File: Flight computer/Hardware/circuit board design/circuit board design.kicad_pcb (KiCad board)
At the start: 4 copper layers, 82.5 x 31.8 mm, 106 parts, among them J1 Conn_01x04, J2 USB_B_Micro, J3 Conn_01x02, Q1 Q_PMOS_DGS, U1 IIS2MDC, U10 BMI088, U11 ATSAML21J18B-AUT, U12 MAX2659ELT+, U13 SAFEB1G57KE0F00, U2 AS179-92LF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

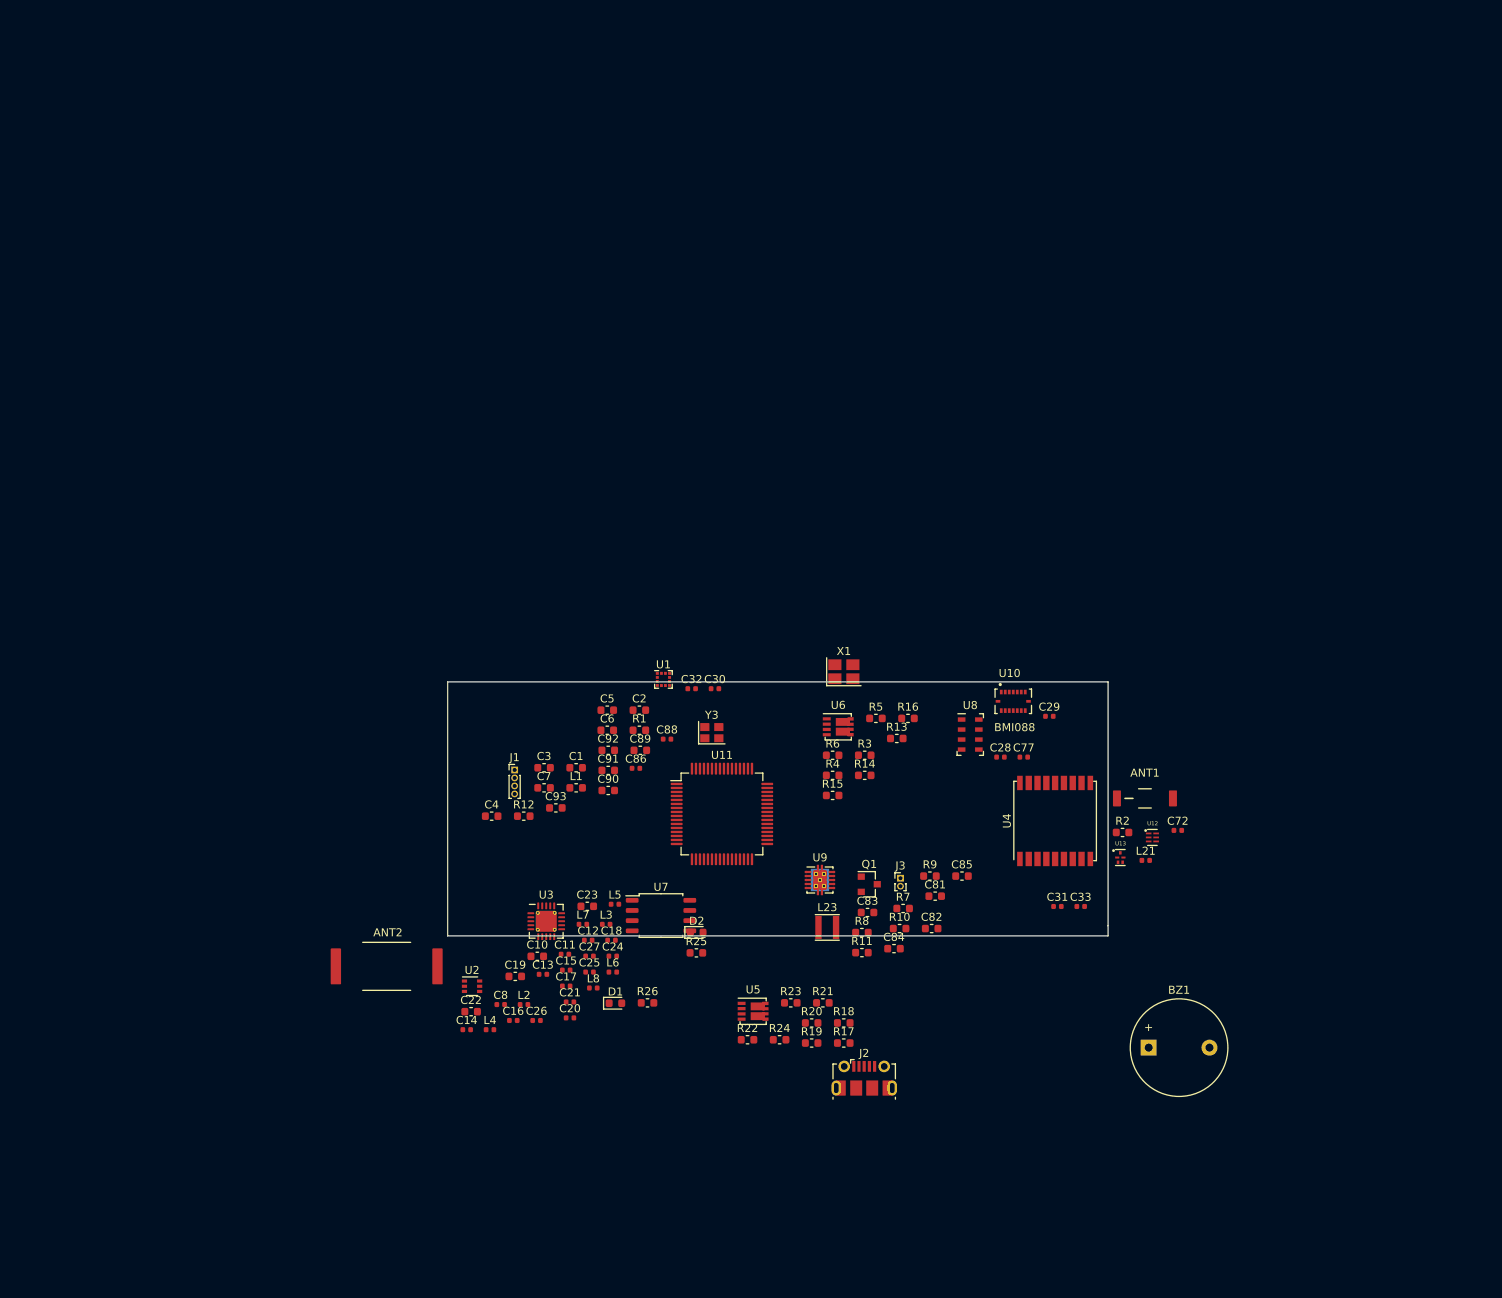
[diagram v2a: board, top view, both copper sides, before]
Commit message: set up the PCB to fit formfactor
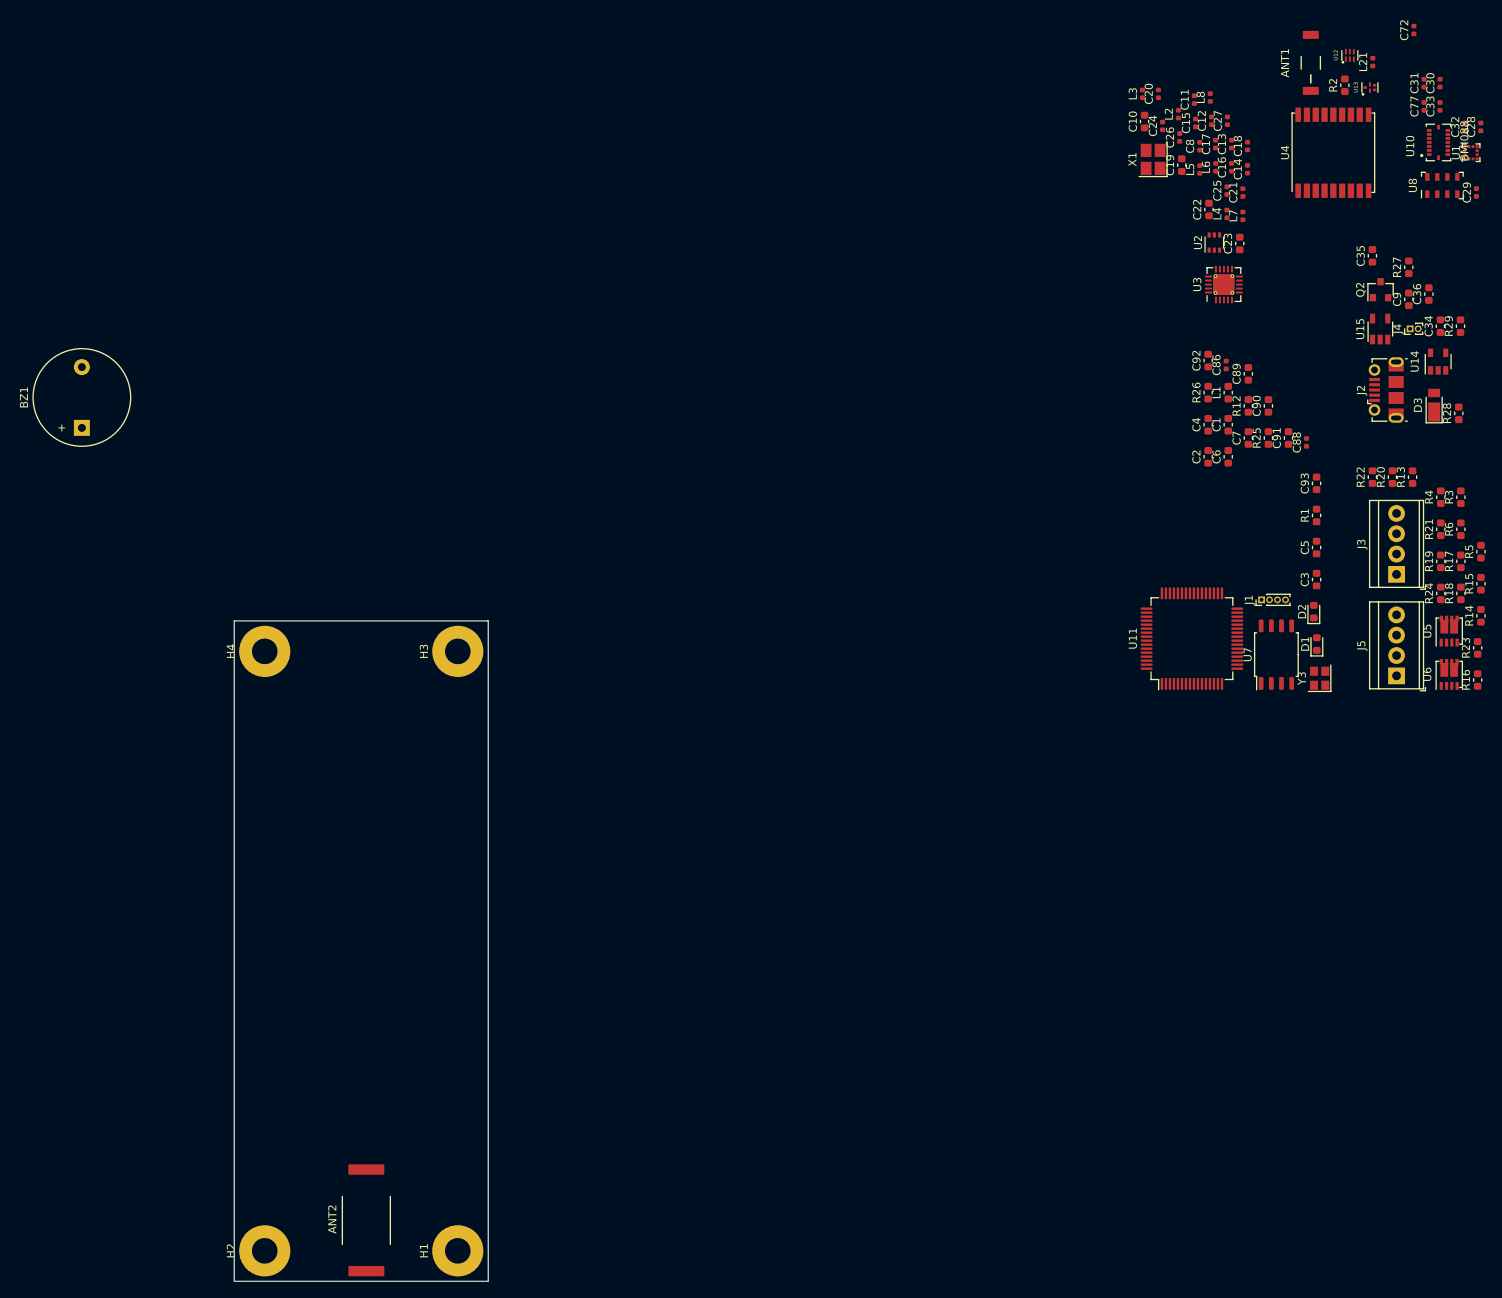
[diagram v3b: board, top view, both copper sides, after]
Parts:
- removed C81, C83, C84: 10uF, Capacitor_SMD:C_0603_1608Metric
- removed C82, C85: 100nF, Capacitor_SMD:C_0603_1608Metric
- removed L23: 2.2uH, Inductor_SMD:L_Taiyo-Yuden_NR-30xx
- removed Q1: Q_PMOS_DGS, Package_TO_SOT_SMD:SOT-23
- removed R10: 180K, Resistor_SMD:R_0603_1608Metric
- removed R11: 10K, Resistor_SMD:R_0603_1608Metric
- removed R7, R8: 100K, Resistor_SMD:R_0603_1608Metric
- removed R9: 1M, Resistor_SMD:R_0603_1608Metric
- removed U9: TPS61200DRC, Package_SON:Texas_S-PVSON-N10_ThermalVias
- added C34: 10nF, Capacitor_SMD:C_0603_1608Metric, F.Cu at (221.9, 31.7)
- added C35: 1uf, Capacitor_SMD:C_0603_1608Metric, F.Cu at (213.4, 22.9)
- added C36: 1uf, Capacitor_SMD:C_0603_1608Metric, F.Cu at (220.4, 27.7)
- added C9: 100nF, Capacitor_SMD:C_0603_1608Metric, F.Cu at (217.9, 28.4)
- added D3: DFLS130L, Diode_SMD:D_PowerDI-123, F.Cu at (221.1, 41.6)
- added H1: MountingHole_Pad, MountingHole:MountingHole_3.2mm_M3_Pad, F.Cu at (99.1, 147.3)
- added H2: MountingHole_Pad, MountingHole:MountingHole_3.2mm_M3_Pad, F.Cu at (74.9, 147.3)
- added H3: MountingHole_Pad, MountingHole:MountingHole_3.2mm_M3_Pad, F.Cu at (99.1, 72.4)
- added H4: MountingHole_Pad, MountingHole:MountingHole_3.2mm_M3_Pad, F.Cu at (74.9, 72.4)
- added J4: Conn_01x02, Connector_PinHeader_1.00mm:PinHeader_1x02_P1.00mm_Vertical, F.Cu at (218.1, 32.1)
- added J5: Screw_Terminal_01x04, TerminalBlock_TE-Connectivity:TerminalBlock_TE_282834-4_1x04_P2.54mm_Horizontal, F.Cu at (216.4, 75.4)
- added Q2: Q_PMOS_DGS, Package_TO_SOT_SMD:SOT-23, F.Cu at (214.4, 27.2)
- added R27: 10K, Resistor_SMD:R_0603_1608Metric, F.Cu at (217.9, 24.4)
- added R28: 100K, Resistor_SMD:R_0603_1608Metric, F.Cu at (224.2, 42.6)
- added R29: 100K, Resistor_SMD:R_0603_1608Metric, F.Cu at (224.4, 31.7)
- added U14: MAX40200AUK, Package_TO_SOT_SMD:SOT-23-5, F.Cu at (221.6, 36.2)
- added U15: LD3985G33R_TSOT23, Package_TO_SOT_SMD:TSOT-23-5, F.Cu at (214.4, 32.1)
- ANT2: value Yageo434 -> ICSSPicoTracker_Yageo434
- J3: value Conn_01x02 -> Screw_Terminal_01x04; footprint Connector_PinHeader_1.00mm:PinHeader_1x02_P1.00mm_Vertical -> TerminalBlock_TE-Connectivity:TerminalBlock_TE_282834-4_1x04_P2.54mm_Horizontal
- moved BZ1 154.2 mm to (52.1, 44.5), turned to 90 degrees
- moved C14 145.2 mm to (197.8, 12.1), turned to 90 degrees
- moved C16 139.4 mm to (195.8, 11.9), turned to 90 degrees
- moved C8 138.4 mm to (191.8, 9.24), turned to 90 degrees
- moved L2 138.1 mm to (189.1, 5.23), turned to 90 degrees
- moved L4 137.4 mm to (195.2, 17.7), turned to 90 degrees
- moved C20 136.9 mm to (186.6, 2.69), turned to 90 degrees
- moved C26 136.6 mm to (189.3, 8.14), turned to 90 degrees
- moved C22 136.2 mm to (193.0, 17.2), turned to 90 degrees
- moved L8 135.4 mm to (193.1, 3.15), turned to 90 degrees
- moved C13 134.8 mm to (195.8, 8.97), turned to 90 degrees
- moved C17 132.9 mm to (193.8, 8.97), turned to 90 degrees
- moved C11 132.7 mm to (191.1, 3.42), turned to 90 degrees
- moved C15 131.9 mm to (191.3, 6.33), turned to 90 degrees
- moved C21 131.6 mm to (197.2, 15.0), turned to 90 degrees
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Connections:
- J3 pad 1: VMEM -> Vdrive
- J3 pad 2: GND -> /pyro_driver/FET_B
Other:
- board size 82.5 x 31.8 mm -> 31.8 x 82.5 mm

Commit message: made some attempts to route the board
-replaced footprint for Radio TCXO
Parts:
- removed C72: 1nF, Capacitor_SMD:C_0402_1005Metric
- removed L21: 6.8nH, Inductor_SMD:L_0402_1005Metric
- BZ1, J3, J5: moved to B.Cu
- X1: footprint Oscillator:Oscillator_SMD_SeikoEpson_SG210-4Pin_2.5x2.0mm_HandSoldering -> Crystal:Crystal_SMD_2520-4Pin_2.5x2.0mm
- moved ANT1 331.9 mm to (273.1, 323.9), turned to 270 degrees
- moved H4 325.1 mm to (279.4, 325.1), turned to 270 degrees
- moved U12 325.0 mm to (273.1, 316.9)
- moved U13 320.2 mm to (270.5, 316.9), turned to 180 degrees
- moved C31 319.3 mm to (268.6, 316.9)
- moved C30 318.8 mm to (267.3, 316.9), turned to 270 degrees
- moved R2 318.1 mm to (271.8, 313.7), turned to 0 degrees
- moved C33 313.5 mm to (267.3, 314.5), turned to 270 degrees
- moved BZ1 311.7 mm to (266.7, 270.5), turned to 270 degrees
- moved C32 310.7 mm to (268.6, 314.5), turned to 270 degrees
- moved C77 309.8 mm to (265.4, 310.7), turned to 270 degrees
- moved U1 308.5 mm to (263.5, 316.2), turned to 270 degrees
- moved U10 308.1 mm to (255.9, 315.0)
- moved U4 302.1 mm to (271.8, 305.4), turned to 270 degrees
- moved U8 299.7 mm to (262.3, 311.1), turned to 180 degrees
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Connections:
- U12 pad 3: Net-(L21-Pad1) -> Net-(ANT1-Pad1)
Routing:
- net Net-(R2-Pad1): track 0.00 -> 6.56 mm
- net Net-(ANT1-Pad1): track 0.00 -> 3.29 mm
- net Net-(U12-Pad6): track 0.00 -> 2.48 mm
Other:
- board size 31.8 x 82.5 mm -> 31.7 x 82.6 mm
- board text added: "Board is 4 layer JLCPCB Type JLC7628 1.6mm overall thickness Layer 1 RF and Signal 1oz copper Insulator .2mm 4.6 dielectric constant Layer 2 Ground 1/2 oz copper Insulator 1.065mm 4.6 dielectric constant Layer 3 Power 1/2oz copper Insulator 0.2mm 4.6 dielectric constant Layer 4 Signal 1oz copper Layer 1-2 50 ohm Microstrip width 11.55mil"

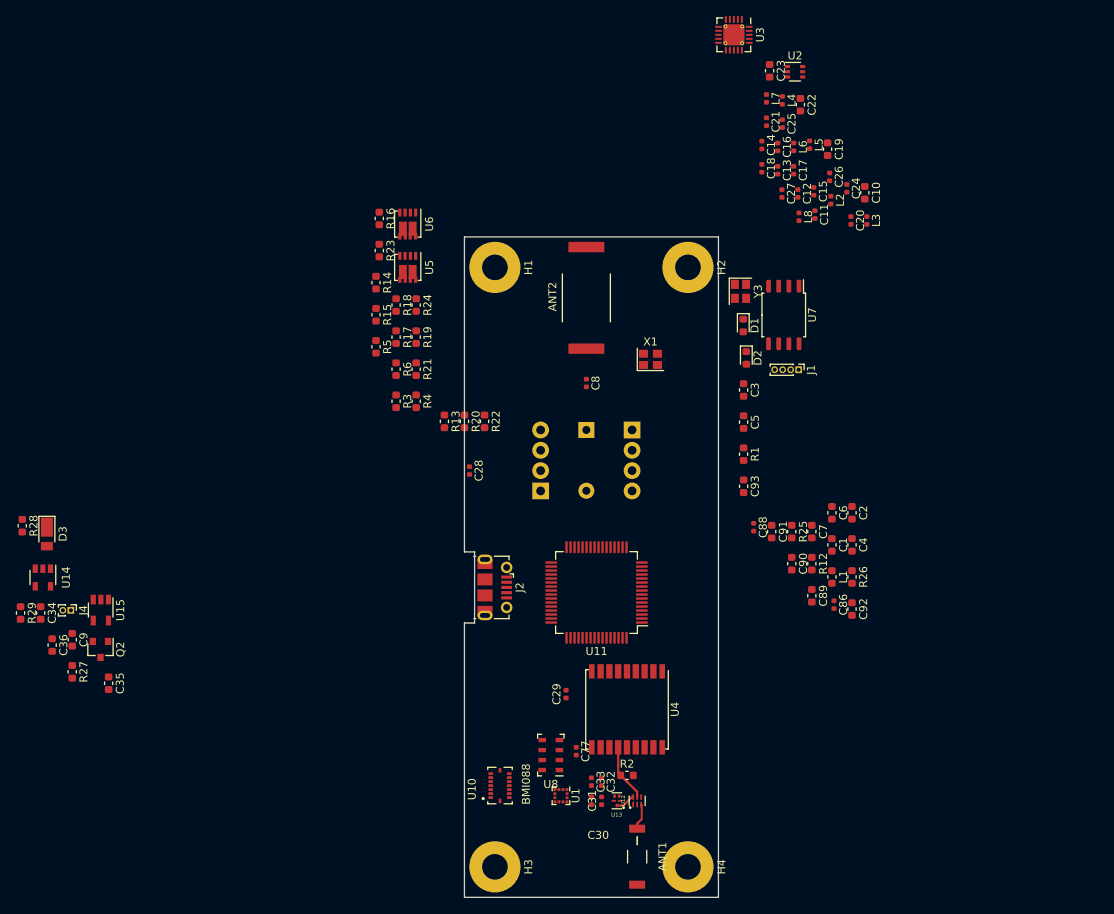
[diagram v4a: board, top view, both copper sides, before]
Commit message: moved reset pin to programming pin header
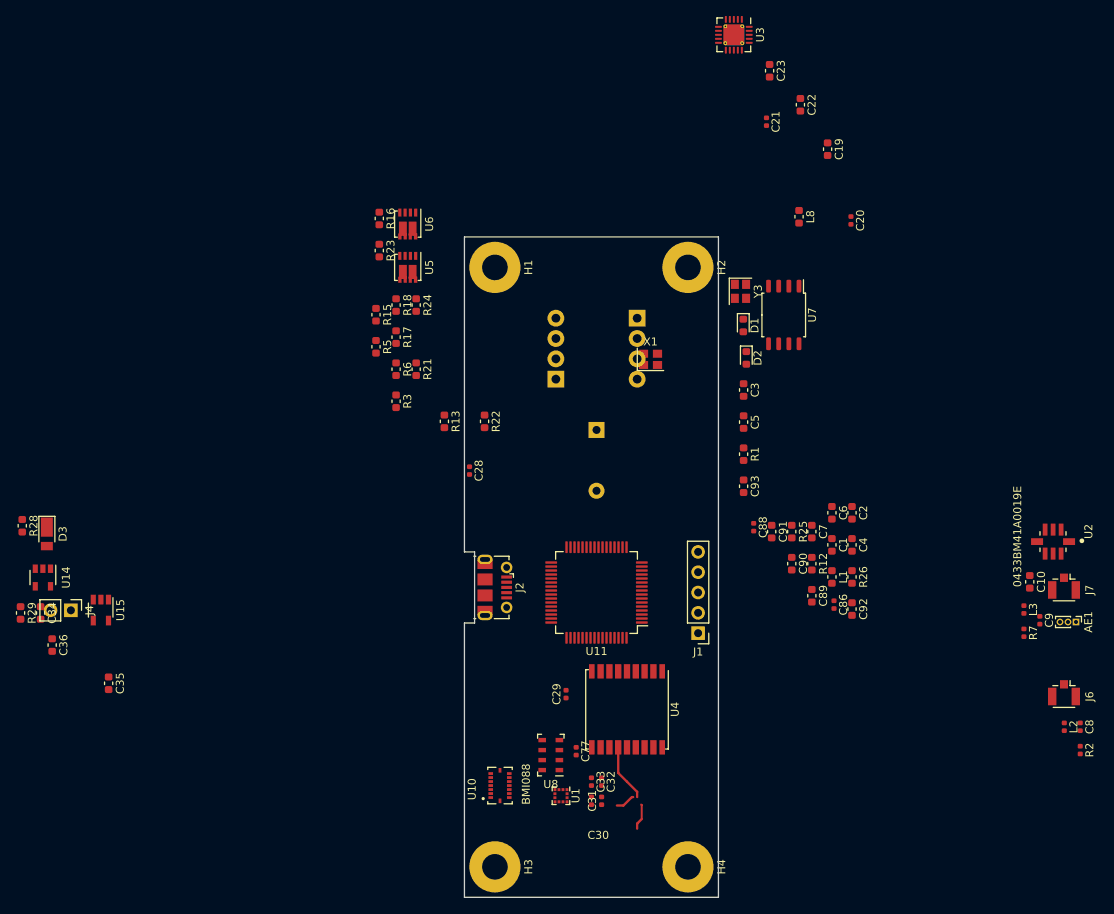
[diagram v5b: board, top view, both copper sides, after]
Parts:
- removed ANT1: Johanson1575, pico_tracker:Johanson1575
- removed ANT2: ICSSPicoTracker_Yageo434, pico_tracker:Yageo434
- removed C11, C12, C13: 150pF, Capacitor_SMD:C_0402_1005Metric
- removed C14: 12pF, Capacitor_SMD:C_0402_1005Metric
- removed C15: 33pF, Capacitor_SMD:C_0402_1005Metric
- removed C16: 15pF, Capacitor_SMD:C_0402_1005Metric
- removed C17, C27: 4.7pF, Capacitor_SMD:C_0402_1005Metric
- removed C18: 9.1pF, Capacitor_SMD:C_0402_1005Metric
- removed C24, C25: 1nF, Capacitor_SMD:C_0402_1005Metric
- removed C26: NF, Capacitor_SMD:C_0402_1005Metric
- removed L4: 30nH, Inductor_SMD:L_0402_1005Metric
- removed L5: 22nH, Inductor_SMD:L_0402_1005Metric
- removed L6, L7: 62nH, Inductor_SMD:L_0402_1005Metric
- removed Q2: Q_PMOS_DGS, Package_TO_SOT_SMD:SOT-23
- removed R14, R19, R20, R4: 100, Resistor_SMD:R_0603_1608Metric
- removed R27: 10K, Resistor_SMD:R_0603_1608Metric
- removed U12: MAX2659ELT+, pico_tracker:uDFN-6_1.0x1.5mm_P0.5mm
- removed U13: SAFEB1G57KE0F00, pico_tracker:Murata SAFE
- added AE1: Antenna, Connector_PinHeader_1.00mm:PinHeader_1x03_P1.00mm_Vertical, F.Cu at (327.9, 294.5)
- added J6: Conn_Coaxial, Connector_Coaxial:U.FL_Hirose_U.FL-R-SMT-1_Vertical, F.Cu at (326.4, 303.4)
- added J7: Conn_Coaxial, Connector_Coaxial:U.FL_Hirose_U.FL-R-SMT-1_Vertical, F.Cu at (326.4, 290.0)
- added R7: NF, Resistor_SMD:R_0402_1005Metric, F.Cu at (321.4, 295.9)
- C10: value 2.2uF -> NF
- C19: value 100nf -> 270pf
- C8: value NF -> 10nF
- C9: value 100nF -> 270pF; footprint Capacitor_SMD:C_0603_1608Metric -> Capacitor_SMD:C_0402_1005Metric
- J1: footprint Connector_PinHeader_1.00mm:PinHeader_1x04_P1.00mm_Vertical -> Connector_PinHeader_2.54mm:PinHeader_1x05_P2.54mm_Vertical
- J4: footprint Connector_PinHeader_1.00mm:PinHeader_1x02_P1.00mm_Vertical -> Connector_PinHeader_2.54mm:PinHeader_1x02_P2.54mm_Vertical
- L2: value 0R -> 27nH; footprint Inductor_SMD:L_0402_1005Metric -> Resistor_SMD:R_0402_1005Metric
- L3: value 18nH -> 0R
- L8: footprint Inductor_SMD:L_0402_1005Metric -> Inductor_SMD:L_0603_1608Metric
- R2: value 10K -> 10 Ohm; footprint Resistor_SMD:R_0603_1608Metric -> Resistor_SMD:R_0402_1005Metric
- U2: value AS179-92LF -> 0433BM41A0019E; footprint Package_TO_SOT_SMD:SOT-363_SC-70-6 -> Johanson_frontend:BALUN_0433BM41A0019E
- moved C9 121.0 mm to (323.4, 294.3)
- moved C8 75.2 mm to (328.4, 307.6)
- moved L2 72.0 mm to (326.4, 307.6)
- moved U2 67.0 mm to (325.0, 284.5), turned to 270 degrees
- moved R2 56.7 mm to (328.4, 310.5), turned to 270 degrees
- moved C10 52.8 mm to (322.1, 289.5)
- moved L3 52.4 mm to (321.4, 293.0)
- moved J1 35.2 mm to (280.7, 295.9), turned to 180 degrees
- moved J5 14.1 mm to (262.9, 264.2)
- moved J3 14.0 mm to (273.1, 256.5)
- moved BZ1 1.27 mm to (268.0, 270.5)
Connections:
- C10 pad 1: +3V3 -> Net-(AE1-Pad1)
- C8 pad 1: Net-(ANT2-Pad1) -> Net-(C8-Pad1)
- C9 pad 1: /MCU/MCU_PA13 -> Net-(C9-Pad1)
- L2 pad 1: Net-(C11-Pad2) -> Net-(C8-Pad1)
- L2 pad 2: Net-(ANT2-Pad1) -> Net-(J6-Pad1)
- L3 pad 1: Net-(C14-Pad1) -> Net-(AE1-Pad1)
- L3 pad 2: Net-(C12-Pad1) -> Net-(C9-Pad1)
- L8 pad 1: Net-(L4-Pad1) -> Net-(L8-Pad1)
- R2 pad 1: Net-(R2-Pad1) -> Net-(C8-Pad1)
- R2 pad 2: GND -> Net-(R2-Pad2)
- R28 pad 1: Net-(Q2-Pad1) -> Vdrive
- U11 pad 30: /MCU/MCU_PA13 -> Net-(U11-Pad30)
- U2 pad 1: Net-(C12-Pad2) -> GND
- U2 pad 2: GND -> Net-(C9-Pad2)
- U2 pad 3: Net-(C13-Pad1) -> GND
- U2 pad 4: Net-(C25-Pad1) -> GND
- U2 pad 5: Net-(C11-Pad1) -> GND
- U2 pad 6: Net-(C24-Pad1) -> Net-(L8-Pad1)
- U3 pad 19: Net-(C24-Pad1) -> Net-(U3-Pad19)
- U3 pad 2: Net-(C17-Pad2) -> Net-(U2-Pad8)
- U3 pad 20: Net-(C25-Pad1) -> Net-(U3-Pad20)
- U3 pad 3: Net-(C27-Pad2) -> Net-(U2-Pad7)
- U3 pad 4: Net-(L4-Pad1) -> Net-(L8-Pad1)
- U4 pad 11: Net-(U13-Pad4) -> Net-(J6-Pad1)
- U4 pad 13: Net-(R2-Pad1) -> Net-(U4-Pad13)
- U4 pad 14: Net-(U12-Pad4) -> Net-(R2-Pad2)
- U5 pad 2: Net-(R19-Pad1) -> /pyro_driver/FIRE_C
- U5 pad 4: Net-(R20-Pad1) -> /pyro_driver/FIRE_D
- U6 pad 2: Net-(R4-Pad1) -> /pyro_driver/FIRE_A
- U6 pad 4: Net-(R14-Pad1) -> /pyro_driver/FIRE_B
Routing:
- net Net-(U4-Pad13): track 0.00 -> 6.56 mm
- net Net-(R2-Pad1): track 6.56 -> 0.00 mm
